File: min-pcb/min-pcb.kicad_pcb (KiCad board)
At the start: 2 copper layers, 38 x 25.5 mm, 10 parts, among them J1 Conn_Pi, J2 Conn_DCDC, J3 Conn_Ext, SW1 SW_Push, U1 74HCT74

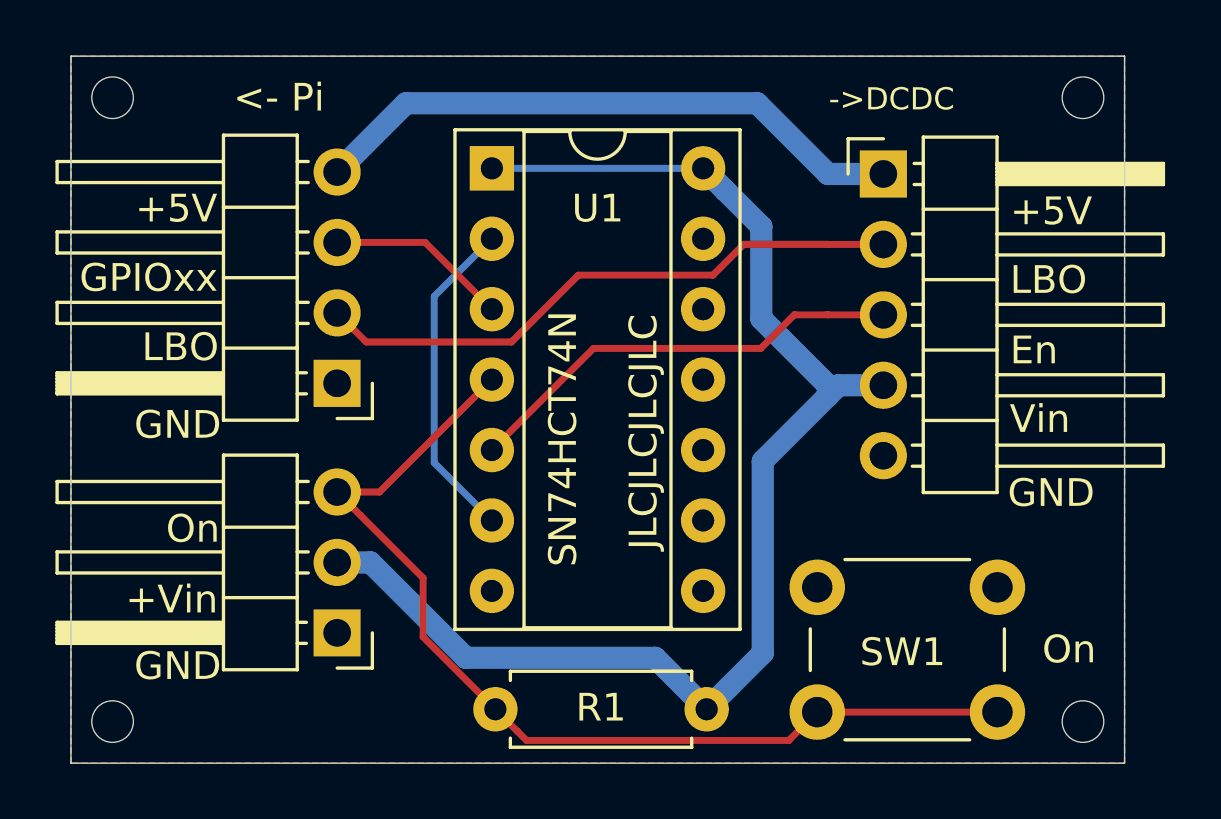
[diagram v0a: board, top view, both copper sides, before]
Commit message: replaced 74HCT74 with 74HC74
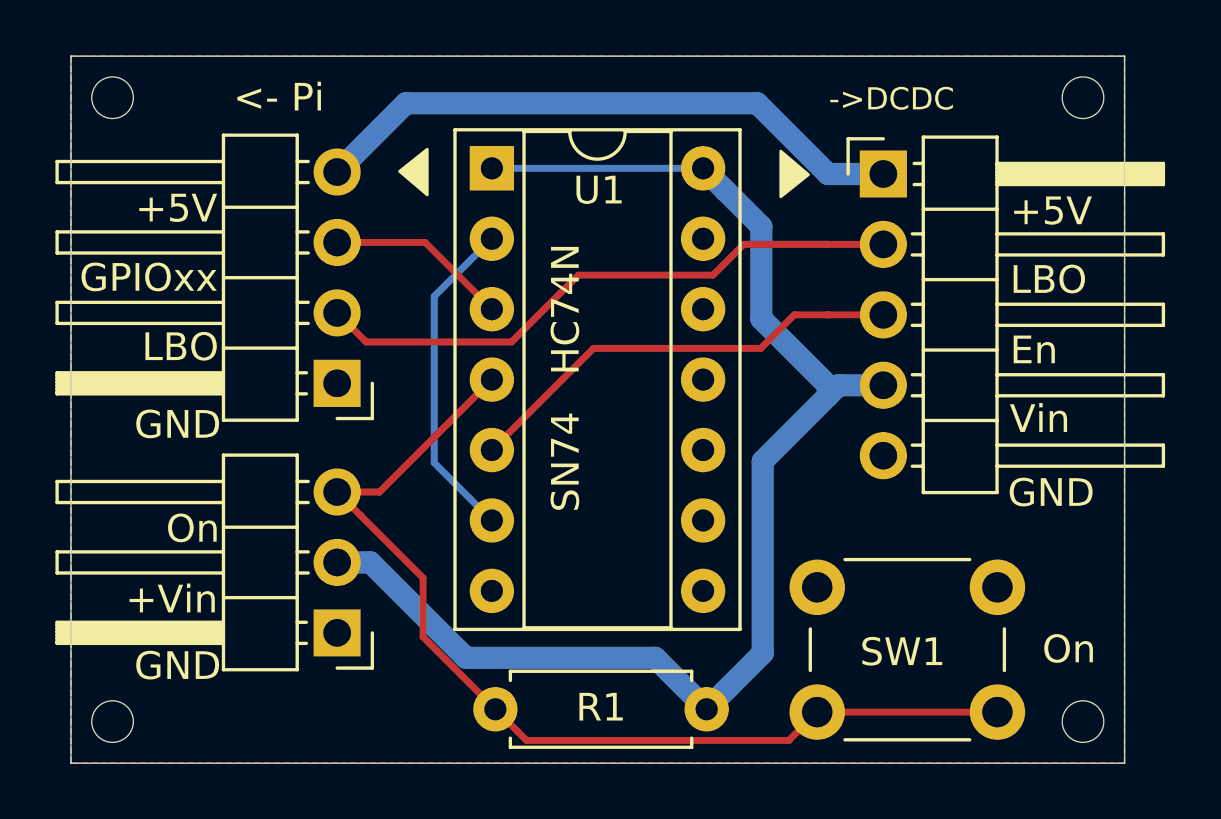
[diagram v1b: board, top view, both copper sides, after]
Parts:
- U1: value 74HCT74 -> 74HC74
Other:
- board text added: "Rev 3"
- board text added: "SN74 HC74N"
- board text removed: "JLCJLCJLCJLC"
- board text removed: "Rev 2"
- board text removed: "SN74HCT74N"

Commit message: bugfix: prevent 2nd flip-flop from floating
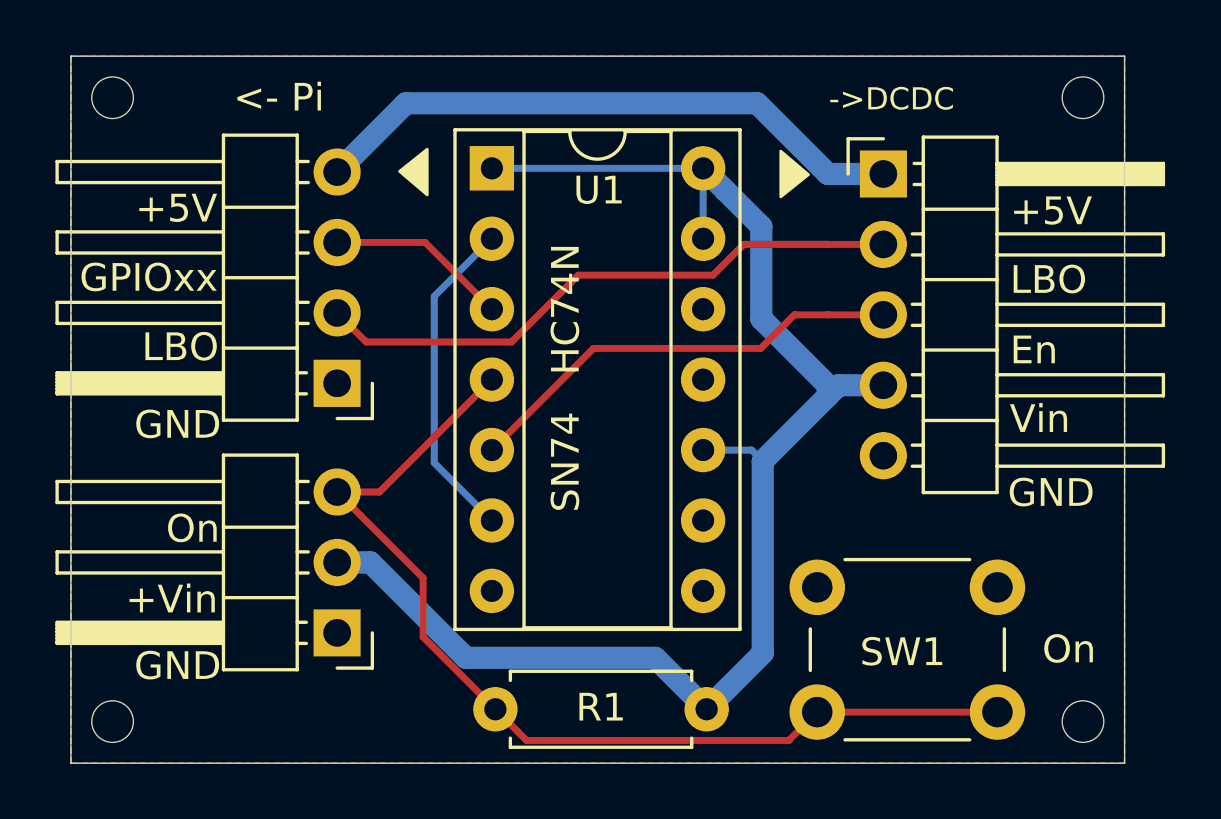
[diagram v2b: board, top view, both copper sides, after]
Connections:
- U1 pad 10: Net-(U1-Pad10) -> /Vin
- U1 pad 11: Net-(U1-Pad11) -> GND
- U1 pad 12: Net-(U1-Pad12) -> GND
- U1 pad 13: Net-(U1-Pad13) -> /Vin
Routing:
- net /Vin: track 48.5 -> 53.3 mm
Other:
- board text added: "Rev 4"
- board text removed: "Rev 3"
